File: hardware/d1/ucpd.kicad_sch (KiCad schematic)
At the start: 50 parts, among them Q1 CSD17577Q3A, Q2 CSD17577Q3A, U15 ESDA25P35-1U1M, U16 ESDA25P35-1U1M, U3 TS3USB221RSER, U4 TCPP03-M20, U5 TCPP03-M20

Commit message: Fix parts
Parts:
- removed C1: 1nF 50V, Capacitor_SMD:C_0402_1005Metric, symbol JLCImport:0402B102K500NT
- removed C23: 4.7uF 16V, Capacitor_SMD:C_0603_1608Metric, symbol JLCImport:CL10A475KO8NNNC
- removed R17: 10mΩ 500mW, Resistor_SMD:R_0805_2012Metric, symbol JLCImport:ERJ6BWFR010V
- added R27: 7mΩ 500mW, Resistor_SMD:R_0805_2012Metric, symbol JLCImport:HOYLR0805-1_2W-7MR-1
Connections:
- net USB_CHR_ISENSE: now also R27.2
- net USB_CHR_VBUS: now also R27.1
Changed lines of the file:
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@@
 	)
 	(symbol
-		(lib_id "JLCImport:CL10A475KO8NNNC")
-		(at 177.8 154.94 0)
-		(unit 1)
-		(body_style 1)
-		(exclude_from_sim no)
-		(in_bom yes)
-		(on_board yes)
-		(in_pos_files yes)
-		(dnp no)
-		(property "Reference" "C23"
-			(at 177.8 149.098 0)
-			(show_name no)
-			(do_not_autoplace no)
-			(effects
-				(font
-					(size 1.27 1.27)
-				)
-			)
-		)
-		(property "Value" "4.7uF 16V"
-			(at 177.8 151.638 0)
-			(show_name no)
-			(do_not_autoplace no)
-			(effects
-				(font
-					(size 1.27 1.27)
-				)
-			)
-		)
-		(property "Footprint" "Capacitor_SMD:C_0603_1608Metric"
-			(at 177.8 154.94 0)
-			(hide yes)
-			(show_name no)
-			(do_not_autoplace no)
-			(effects
-				(font
-					(size 1.27 1.27)
-				)
-			)
-		)
-		(property "Datasheet" "https://www.lcsc.com/datasheet/lcsc_datasheet_2304140030_Samsung-Electro-Mechanics-CL10A475KO8NNNC_C19666.pdf"
-			(at 177.8 154.94 0)
-			(hide yes)
-			(show_name no)
-			(do_not_autoplace no)
-			(effects
-				(font
-					(size 1.27 1.27)
-				)
-			)
-		)
-		(property "Description" "16V 4.7uF X5R ±10% 0603 Multilayer Ceramic Capacitors MLCC - SMD/SMT ROHS"
-			(at 177.8 154.94 0)
-			(hide yes)
-			(show_name no)
-			(do_not_autoplace no)
-			(effects
-				(font
-					(size 1.27 1.27)
-				)
-			)
-		)
-		(property "LCSC" "C19666"
-			(at 177.8 154.94 0)
-			(hide yes)
-			(show_name no)
-			(do_not_autoplace no)
-			(effects
-				(font
-					(size 1.27 1.27)
-				)
-			)
-		)
-		(property "Manufacturer" "Samsung Electro-Mechanics"
-			(at 177.8 154.94 0)
-			(hide yes)
-			(show_name no)
-			(do_not_autoplace no)
-			(effects
-				(font
-					(size 1.27 1.27)
-				)
-			)
-		)
-		(property "Manufacturer Part" "CL10A475KO8NNNC"
-			(at 177.8 154.94 0)
-			(hide yes)
-			(show_name no)
-			(do_not_autoplace no)
-			(effects
-				(font
-					(size 1.27 1.27)
-				)
-			)
-		)
-		(pin "2"
-		)
-		(pin "1"
-		)
-		(instances
-			(project "DrunkEarPhoneAdapter"
-				(path "/df940915-8af0-46f9-b18a-23d4684ae671/5c561383-fdd0-44ae-83ac-568aac0f03a9"
-					(reference "C23")
-					(unit 1)
-				)
-			)
-		)
-	)
-	(symbol
 		(lib_id "JLCImport:0603WAF5490T5E")
 		(at 16.51 139.7 90)
@@
 	)
 	(symbol
-		(lib_id "JLCImport:0402B102K500NT")
-		(at 270.51 111.76 0)
-		(unit 1)
-		(body_style 1)
-		(exclude_from_sim no)
-		(in_bom yes)
-		(on_board yes)
-		(in_pos_files yes)
-		(dnp no)
-		(property "Reference" "C1"
-			(at 270.51 106.172 0)
-			(show_name no)
-			(do_not_autoplace no)
-			(effects
-				(font
-					(size 1.27 1.27)
-				)
-			)
-		)
-		(property "Value" "1nF 50V"
-			(at 270.51 108.712 0)
-			(show_name no)
-			(do_not_autoplace no)
-			(effects
-				(font
-					(size 1.27 1.27)
-				)
-			)
-		)
-		(property "Footprint" "Capacitor_SMD:C_0402_1005Metric"
-			(at 270.51 111.76 0)
-			(hide yes)
-			(show_name no)
-			(do_not_autoplace no)
-			(effects
-				(font
-					(size 1.27 1.27)
-				)
-			)
-		)
-		(property "Datasheet" "https://www.lcsc.com/datasheet/lcsc_datasheet_2304140030_FH--Guangdong-Fenghua-Advanced-Tech-0402B102K500NT_C1523.pdf"
-			(at 270.51 111.76 0)
-			(hide yes)
-			(show_name no)
-			(do_not_autoplace no)
-			(effects
-				(font
-					(size 1.27 1.27)
-				)
-			)
-		)
-		(property "Description" "1nF 50V X7R ±10% 0402 Multilayer Ceramic Capacitors MLCC - SMD/SMT ROHS"
-			(at 270.51 111.76 0)
-			(hide yes)
-			(show_name no)
-			(do_not_autoplace no)
-			(effects
-				(font
-					(size 1.27 1.27)
-				)
-			)
-		)
-		(property "LCSC" "C1523"
-			(at 270.51 111.76 0)
-			(hide yes)
-			(show_name no)
-			(do_not_autoplace no)
-			(effects
-				(font
-					(size 1.27 1.27)
-				)
-			)
-		)
-		(property "Manufacturer" "FH (Guangdong Fenghua Advanced Tech)"
-			(at 270.51 111.76 0)
-			(hide yes)
-			(show_name no)
-			(do_not_autoplace no)
-			(effects
-				(font
-					(size 1.27 1.27)
-				)
-			)
-		)
-		(property "Manufacturer Part" "0402B102K500NT"
-			(at 270.51 111.76 0)
-			(hide yes)
-			(show_name no)
-			(do_not_autoplace no)
-			(effects
-				(font
-					(size 1.27 1.27)
-				)
-			)
-		)
-		(pin "1"
-		)
-		(pin "2"
-		)
-		(instances
-			(project "DrunkEarPhoneAdapter"
-				(path "/df940915-8af0-46f9-b18a-23d4684ae671/5c561383-fdd0-44ae-83ac-568aac0f03a9"
-					(reference "C1")
-					(unit 1)
-				)
-			)
-		)
-	)
-	(symbol
 		(lib_id "power:GND")
 		(at 201.93 226.06 0)
@@
 	)
 	(symbol
+		(lib_id "JLCImport:HOYLR0805-1_2W-7MR-1")
+		(at 67.31 36.83 0)
+		(unit 1)
+		(body_style 1)
+		(exclude_from_sim no)
+		(in_bom yes)
+		(on_board yes)
+		(in_pos_files yes)
+		(dnp no)
+		(fields_autoplaced yes)
+		(property "Reference" "R27"
+			(at 67.31 30.48 0)
+			(show_name no)
+			(do_not_autoplace no)
+			(effects
+				(font
+					(size 1.27 1.27)
+				)
+			)
+		)
+		(property "Value" "7mΩ 500mW"
+			(at 67.31 33.02 0)
+			(show_name no)
+			(do_not_autoplace no)
+			(effects
+				(font
+					(size 1.27 1.27)
+				)
+			)
+		)
+		(property "Footprint" "Resistor_SMD:R_0805_2012Metric"
+			(at 67.31 36.83 0)
+			(hide yes)
+			(show_name no)
+			(do_not_autoplace no)
+			(effects
+				(font
+					(size 1.27 1.27)
+				)
+			)
+		)
+		(property "Datasheet" "https://www.lcsc.com/datasheet/lcsc_datasheet_2406041542_Milliohm-HoYLR0805-1-2W-7mR-1-_C22450691.pdf"
+			(at 67.31 36.83 0)
+			(hide yes)
+			(show_name no)
+			(do_not_autoplace no)
+			(effects
+				(font
+					(size 1.27 1.27)
+				)
+			)
+		)
+		(property "Description" "500mW 7mΩ Current Sense Resistor Surface Mount ±1% ±50ppm/℃ 0805 Current Sense Resistors / Shunt Resistors ROHS"
+			(at 67.31 36.83 0)
+			(hide yes)
+			(show_name no)
+			(do_not_autoplace no)
+			(effects
+				(font
+					(size 1.27 1.27)
+				)
+			)
+		)
+		(property "LCSC" "C22450691"
+			(at 67.31 36.83 0)
+			(hide yes)
+			(show_name no)
+			(do_not_autoplace no)
+			(effects
+				(font
+					(size 1.27 1.27)
+				)
+			)
+		)
+		(property "Manufacturer" "Milliohm"
+			(at 67.31 36.83 0)
+			(hide yes)
+			(show_name no)
+			(do_not_autoplace no)
+			(effects
+				(font
+					(size 1.27 1.27)
+				)
+			)
+		)
+		(property "Manufacturer Part" "HoYLR0805-1/2W-7mR-1%"
+			(at 67.31 36.83 0)
+			(hide yes)
+			(show_name no)
+			(do_not_autoplace no)
+			(effects
+				(font
+					(size 1.27 1.27)
+				)
+			)
+		)
+		(pin "1"
+		)
+		(pin "2"
+		)
+		(instances
+			(project "DrunkEarPhoneAdapter"
+				(path "/df940915-8af0-46f9-b18a-23d4684ae671/5c561383-fdd0-44ae-83ac-568aac0f03a9"
+					(reference "R27")
+					(unit 1)
+				)
+			)
+		)
+	)
+	(symbol
 		(lib_id "JLCImport:CL05B104KB54PNC")
 		(at 107.95 102.87 90)
@@
 					(unit 1)
 				)
-			)
-		)
-	)
-	(symbol
-		(lib_id "JLCImport:ERJ6BWFR010V")
-		(at 67.31 36.83 0)
-		(unit 1)
-		(body_style 1)
-		(exclude_from_sim no)
-		(in_bom yes)
-		(on_board yes)
-		(in_pos_files yes)
-		(dnp no)
-		(fields_autoplaced yes)
-		(property "Reference" "R17"
-			(at 67.31 30.48 0)
-			(show_name no)
-			(do_not_autoplace no)
-			(effects
-				(font
-					(size 1.27 1.27)
-				)
-			)
-		)
-		(property "Value" "10mΩ 500mW"
-			(at 67.31 33.02 0)
-			(show_name no)
-			(do_not_autoplace no)
-			(effects
-				(font
-					(size 1.27 1.27)
-				)
-			)
-		)
-		(property "Footprint" "Resistor_SMD:R_0805_2012Metric"
-			(at 67.31 36.83 0)
-			(hide yes)
-			(show_name no)
-			(do_not_autoplace no)
-			(effects
-				(font
-					(size 1.27 1.27)
-				)
-			)
-		)
-		(property "Datasheet" "https://item.szlcsc.com/142685.html"
-			(at 67.31 36.83 0)
-			(hide yes)
-			(show_name no)
-			(do_not_autoplace no)
-			(effects
-				(font
-					(size 1.27 1.27)
-				)
-			)
-		)
-		(property "Description" "-55℃~+155℃ 0ppm/℃~+300ppm/℃ 10mΩ 500mW Thick Film Resistor ±1% 0805 Chip Resistor - Surface Mount ROHS"
-			(at 67.31 36.83 0)
-			(hide yes)
-			(show_name no)
-			(do_not_autoplace no)
-			(effects
-				(font
-					(size 1.27 1.27)
-				)
-			)
-		)
-		(property "LCSC" "C409060"
-			(at 67.31 36.83 0)
-			(hide yes)
-			(show_name no)
-			(do_not_autoplace no)
-			(effects
-				(font
-					(size 1.27 1.27)
-				)
-			)
-		)
-		(property "Manufacturer" "PANASONIC"
-			(at 67.31 36.83 0)
-			(hide yes)
-			(show_name no)
-			(do_not_autoplace no)
-			(effects
-				(font
-					(size 1.27 1.27)
-				)
-			)
-		)
-		(property "Manufacturer Part" "ERJ6BWFR010V"
-			(at 67.31 36.83 0)
-			(hide yes)
-			(show_name no)
-			(do_not_autoplace no)
-			(effects
-				(font
-					(size 1.27 1.27)
-				)
-			)
-		)
-		(pin "2"
-		)
-		(pin "1"
-		)
-		(instances
-			(project "DrunkEarPhoneAdapter"
-				(path "/df940915-8af0-46f9-b18a-23d4684ae671/5c561383-fdd0-44ae-83ac-568aac0f03a9"
-					(reference "R17")
-					(unit 1)
-				)

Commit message: Trace
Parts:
- removed USBC2: (no value), JLCImport:USBC_EXT_5P, symbol JLCImport:USBC_5P_EXT
- added USBC3, USBC4: (no value), JLCImport:USBC_EXT_5P, symbol JLCImport:USBC_5P_EXT
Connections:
- net GND: now also USBC3.5 (GND), USBC4.5 (GND)
- net USB_PHONE_CC1: now also USBC3.4 (CC), USBC4.4 (CC)
- net USB_PHONE_VBUS: now also USBC3.1 (VBUS), USBC4.1 (VBUS)
- net D_P: now reaches L7.5 (D-)
- net D_P: now also USBC3.2 (D-), USBC4.2 (D-)
- net D_N: now reaches L7.6 (D+)
- net D_N: now also USBC3.3 (D+), USBC4.3 (D+)
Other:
- moved on the sheet: L7

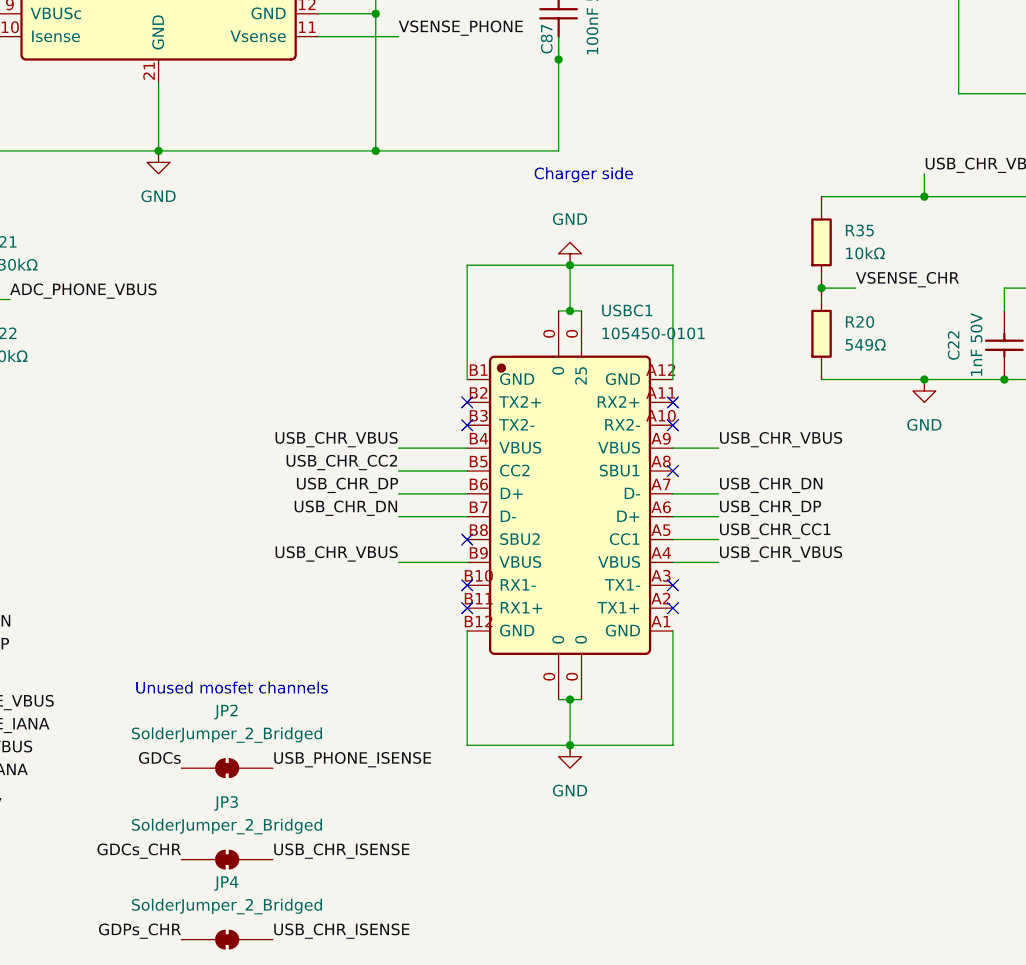
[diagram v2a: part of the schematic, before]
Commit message: Replace USB
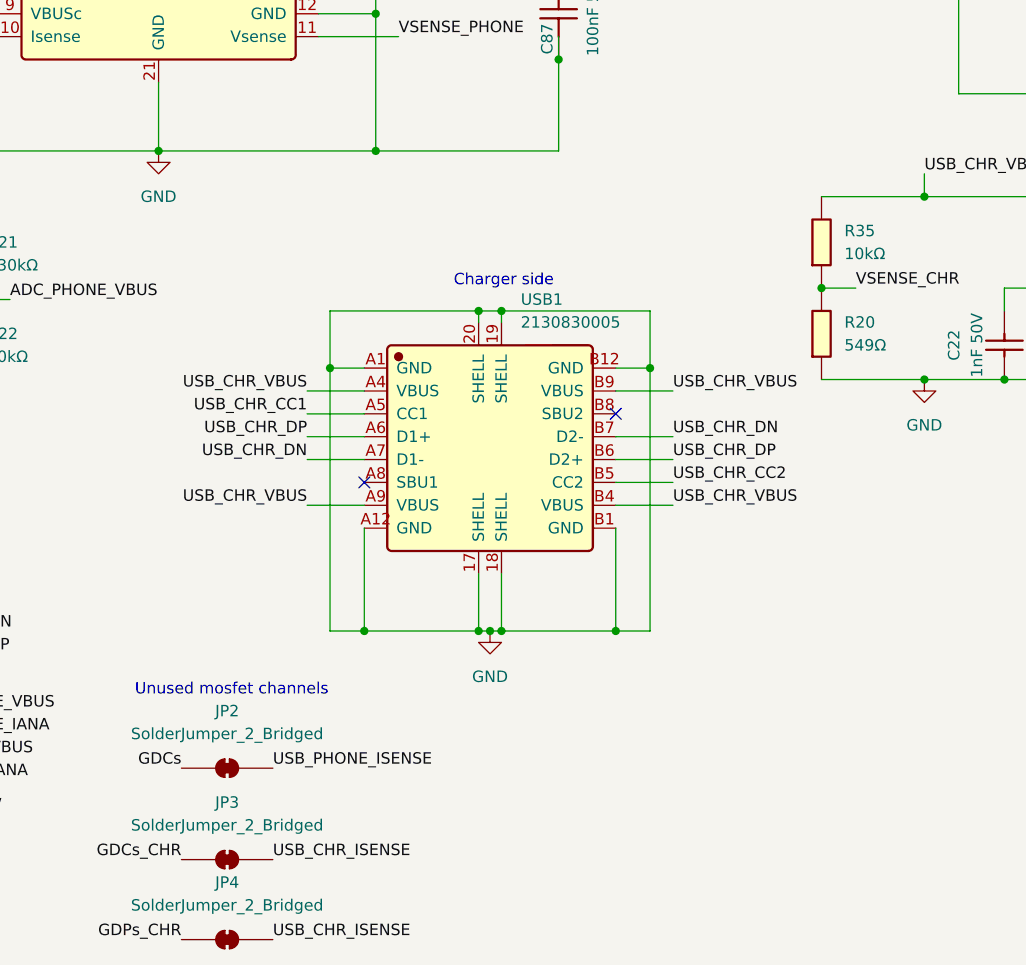
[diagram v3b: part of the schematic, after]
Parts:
- removed USBC1: 105450-0101, JLCImport:105450-0101, symbol JLCImport:105450-0101
- added USB1: 2130830005, JLCImport:2130830005, symbol JLCImport:2130830005
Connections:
- net GND: now also USB1.17 (SHELL), USB1.18 (SHELL), USB1.19 (SHELL), USB1.20 (SHELL), USB1.A1 (GND), USB1.A12 (GND), USB1.B1 (GND), USB1.B12 (GND)
- net USB_CHR_CC1: now also USB1.A5 (CC1)
- net USB_CHR_CC2: now also USB1.B5 (CC2)
- net USB_CHR_DN: now also USB1.A7 (D1-), USB1.B7 (D2-)
- net USB_CHR_DP: now also USB1.A6 (D1+), USB1.B6 (D2+)
- net USB_CHR_VBUS: now also USB1.A4 (VBUS), USB1.A9 (VBUS), USB1.B4 (VBUS), USB1.B9 (VBUS)
- no-connect marks 15 -> 7

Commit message: Traces
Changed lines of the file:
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@@
 		)
 	)
-	(label "UCPD2_CC2"
-		(at 186.69 88.9 180)
-		(effects
-			(font
-				(size 1.27 1.27)
-			)
-			(justify right bottom)
-		)
-	)
 	(label "USB_CHR_CC2"
 		(at 120.65 154.94 0)
@@
 		)
 	)
-	(label "UCPD2_CC1"
-		(at 186.69 83.82 180)
-		(effects
-			(font
-				(size 1.27 1.27)
-			)
-			(justify right bottom)
-		)
-	)
 	(label "USB_CHR_SAFE_DP"
 		(at 85.09 228.6 0)
@@
 		)
 	)
+	(label "UCPD2_CC1"
+		(at 186.69 83.82 180)
+		(effects
+			(font
+				(size 1.27 1.27)
+			)
+			(justify right bottom)
+		)
+	)
 	(label "USB_CHR_DN"
 		(at 120.65 149.86 0)
@@
 		)
 	)
+	(label "UCPD2_CC2"
+		(at 186.69 88.9 180)
+		(effects
+			(font
+				(size 1.27 1.27)
+			)
+			(justify right bottom)
+		)
+	)
 	(label "ADC_CHR_VBUS"
 		(at 35.56 185.42 0)
@@
 	)
 	(symbol
+		(lib_id "JLCImport:USBC_5P_EXT")
+		(at 138.43 269.24 0)
+		(unit 1)
+		(body_style 1)
+		(exclude_from_sim no)
+		(in_bom no)
+		(on_board yes)
+		(in_pos_files no)
+		(dnp no)
+		(fields_autoplaced yes)
+		(property "Reference" "USBC4"
+			(at 143.51 269.2399 0)
+			(show_name no)
+			(do_not_autoplace no)
+			(effects
+				(font
+					(size 1.27 1.27)
+				)
+				(justify left)
+			)
+		)
+		(property "Value" ""
+			(at 138.43 269.24 0)
+			(show_name no)
+			(do_not_autoplace no)
+			(effects
+				(font
+					(size 1.27 1.27)
+				)
+			)
+		)
+		(property "Footprint" "JLCImport:USBC_EXT_5P"
+			(at 138.43 269.24 0)
+			(hide yes)
+			(show_name no)
+			(do_not_autoplace no)
+			(effects
+				(font
+					(size 1.27 1.27)
+				)
+			)
+		)
+		(property "Datasheet" ""
+			(at 138.43 269.24 0)
+			(hide yes)
+			(show_name no)
+			(do_not_autoplace no)
+			(effects
+				(font
+					(size 1.27 1.27)
+				)
+			)
+		)
+		(property "Description" ""
+			(at 138.43 269.24 0)
+			(hide yes)
+			(show_name no)
+			(do_not_autoplace no)
+			(effects
+				(font
+					(size 1.27 1.27)
+				)
+			)
+		)
+		(pin "2"
+		)
+		(pin "5"
+		)
+		(pin "4"
+		)
+		(pin "3"
+		)
+		(pin "1"
+		)
+		(instances
+			(project "DrunkEarPhoneAdapter"
+				(path "/df940915-8af0-46f9-b18a-23d4684ae671/5c561383-fdd0-44ae-83ac-568aac0f03a9"
+					(reference "USBC4")
+					(unit 1)
+				)
+			)
+		)
+	)
+	(symbol
 		(lib_id "JLCImport:0402WGF1001TCE")
 		(at 157.48 90.17 0)
@@
 					(unit 1)
 				)
-			)
-		)
-	)
-	(symbol
-		(lib_id "JLCImport:USBC_5P_EXT")
-		(at 138.43 250.19 0)
-		(unit 1)
-		(body_style 1)
-		(exclude_from_sim no)
-		(in_bom no)
-		(on_board yes)
-		(in_pos_files no)
-		(dnp no)
-		(fields_autoplaced yes)
-		(property "Reference" "USBC4"
-			(at 143.51 250.1899 0)
-			(show_name no)
-			(do_not_autoplace no)
-			(effects
-				(font
-					(size 1.27 1.27)
-				)
-				(justify left)
-			)
-		)
-		(property "Value" ""
-			(at 138.43 250.19 0)
-			(show_name no)
-			(do_not_autoplace no)
-			(effects
-				(font
-					(size 1.27 1.27)
-				)
-			)
-		)
-		(property "Footprint" "JLCImport:USBC_EXT_5P"
-			(at 138.43 250.19 0)
-			(hide yes)
-			(show_name no)
-			(do_not_autoplace no)
-			(effects
-				(font
-					(size 1.27 1.27)
-				)
-			)
-		)
-		(property "Datasheet" ""
-			(at 138.43 250.19 0)
-			(hide yes)
-			(show_name no)
-			(do_not_autoplace no)
-			(effects
-				(font
-					(size 1.27 1.27)
-				)
-			)
-		)
-		(property "Description" ""
-			(at 138.43 250.19 0)
-			(hide yes)
-			(show_name no)
-			(do_not_autoplace no)
-			(effects
-				(font
-					(size 1.27 1.27)
-				)
-			)
-		)
-		(pin "2"
-		)
-		(pin "5"
-		)
-		(pin "4"
-		)
-		(pin "3"
-		)
-		(pin "1"
-		)
-		(instances
-			(project "DrunkEarPhoneAdapter"
-				(path "/df940915-8af0-46f9-b18a-23d4684ae671/5c561383-fdd0-44ae-83ac-568aac0f03a9"
-					(reference "USBC4")
-					(unit 1)
-				)

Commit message: Almost done tracing
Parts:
- removed C33: 330pF 50V, Capacitor_SMD:C_0603_1608Metric, symbol JLCImport:CL10C331JB8NNNC
- removed C66: 10nF 50V X7R, Capacitor_SMD:C_0402_1005Metric, symbol JLCImport:CL05B103KB5NNNC
- removed JP2, JP3, JP4: SolderJumper_2_Bridged, Jumper:SolderJumper-2_P1.3mm_Bridged_RoundedPad1.0x1.5mm, symbol Jumper:SolderJumper_2_Bridged
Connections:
- net GDCs: no longer names the net of U4.8 (GDCs)
- net GDCs_CHR: no longer names the net of U5.8 (GDCs)
- net GDPs_CHR: no longer names the net of U5.6 (GDPs)
- net USB_PHONE_CC2: no longer names the net of U4.13 (CC2c)
- no-connect marks 7 -> 11
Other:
- note removed: "Unused mosfet channels"

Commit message: Fixes
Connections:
- net D_N: now also L7.5 (D-), USBC3.2 (D-), USBC4.2 (D-); no longer L7.6 (D+), USBC3.3 (D+), USBC4.3 (D+)
- net D_P: now also L7.6 (D+), USBC3.3 (D+), USBC4.3 (D+); no longer L7.5 (D-), USBC3.2 (D-), USBC4.2 (D-)
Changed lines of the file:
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@@
 		)
 	)
-	(label "D_N"
+	(label "D_P"
 		(at 77.47 250.19 0)
 		(effects
@@
 		)
 	)
-	(label "D_P"
+	(label "D_N"
 		(at 77.47 252.73 0)
 		(effects

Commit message: Route fixes
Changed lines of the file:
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@@
 	(text "Phone side"
 		(exclude_from_sim no)
-		(at 116.332 241.046 0)
+		(at 123.698 258.826 0)
 		(effects
 			(font
@@
 	)
 	(junction
-		(at 88.9 252.73)
-		(diameter 0)
-		(color 0 0 0 0)
-	)
-	(junction
 		(at 41.91 36.83)
 		(diameter 0)
@@
 	)
 	(junction
-		(at 97.79 250.19)
-		(diameter 0)
-		(color 0 0 0 0)
-	)
-	(junction
 		(at 214.63 111.76)
 		(diameter 0)
@@
 	(wire
 		(pts
-			(xy 97.79 250.19) (xy 130.81 250.19)
-		)
-		(stroke
-			(width 0)
-			(type default)
-		)
-	)
-	(wire
-		(pts
 			(xy 182.88 217.17) (xy 186.69 217.17)
 		)
@@
 	(wire
 		(pts
-			(xy 88.9 247.65) (xy 130.81 247.65)
-		)
-		(stroke
-			(width 0)
-			(type default)
-		)
-	)
-	(wire
-		(pts
 			(xy 41.91 63.5) (xy 49.53 63.5)
 		)
@@
 	(wire
 		(pts
-			(xy 88.9 247.65) (xy 88.9 252.73)
-		)
-		(stroke
-			(width 0)
-			(type default)
-		)
-	)
-	(wire
-		(pts
 			(xy 237.49 101.6) (xy 232.41 101.6)
 		)
@@
 	(wire
 		(pts
-			(xy 109.22 252.73) (xy 130.81 252.73)
-		)
-		(stroke
-			(width 0)
-			(type default)
-		)
-	)
-	(wire
-		(pts
 			(xy 203.2 146.05) (xy 203.2 147.32)
 		)
@@
 	(wire
 		(pts
-			(xy 109.22 255.27) (xy 130.81 255.27)
-		)
-		(stroke
-			(width 0)
-			(type default)
-		)
-	)
-	(wire
-		(pts
 			(xy 241.3 111.76) (xy 214.63 111.76)
 		)
@@
 	(wire
 		(pts
-			(xy 109.22 245.11) (xy 130.81 245.11)
-		)
-		(stroke
-			(width 0)
-			(type default)
-		)
-	)
-	(wire
-		(pts
 			(xy 148.59 143.51) (xy 157.48 143.51)
 		)
@@
 		)
 	)
-	(label "USB_PHONE_CC1"
-		(at 109.22 252.73 180)
-		(effects
-			(font
-				(size 1.27 1.27)
-			)
-			(justify right bottom)
-		)
-	)
 	(label "USB_PHONE_SAFE_DN"
 		(at 208.28 214.63 0)
@@
 		)
 	)
-	(label "USB_PHONE_VBUS"
-		(at 109.22 245.11 180)
-		(effects
-			(font
-				(size 1.27 1.27)
-			)
-			(justify right bottom)
-		)
-	)
 	(label "USB_STM_DN"
 		(at 35.56 171.45 0)
@@
 					(unit 1)
 				)
-			)
-		)
-	)
-	(symbol
-		(lib_id "power:GND")
-		(at 109.22 255.27 0)
-		(unit 1)
-		(body_style 1)
-		(exclude_from_sim no)
-		(in_bom yes)
-		(on_board yes)
-		(in_pos_files yes)
-		(dnp no)
-		(fields_autoplaced yes)
-		(property "Reference" "#PWR063"
-			(at 109.22 261.62 0)
-			(hide yes)
-			(show_name no)
-			(do_not_autoplace no)
-			(effects
-				(font
-					(size 1.27 1.27)
-				)
-			)
-		)
-		(property "Value" "GND"
-			(at 109.22 260.35 0)
-			(show_name no)
-			(do_not_autoplace no)
-			(effects
-				(font
-					(size 1.27 1.27)
-				)
-			)
-		)
-		(property "Footprint" ""
-			(at 109.22 255.27 0)
-			(hide yes)
-			(show_name no)
-			(do_not_autoplace no)
-			(effects
-				(font
-					(size 1.27 1.27)
-				)
-			)
-		)
-		(property "Datasheet" ""
-			(at 109.22 255.27 0)
-			(hide yes)
-			(show_name no)
-			(do_not_autoplace no)
-			(effects
-				(font
-					(size 1.27 1.27)
-				)
-			)
-		)
-		(property "Description" "Power symbol creates a global label with name \"GND\" , ground"
-			(at 109.22 255.27 0)
-			(hide yes)
-			(show_name no)
-			(do_not_autoplace no)
-			(effects
-				(font
-					(size 1.27 1.27)
-				)
-			)
-		)
-		(pin "1"
-		)
-		(instances
-			(project "DrunkEarPhoneAdapter"
-				(path "/df940915-8af0-46f9-b18a-23d4684ae671/5c561383-fdd0-44ae-83ac-568aac0f03a9"
-					(reference "#PWR063")
-					(unit 1)
-				)
